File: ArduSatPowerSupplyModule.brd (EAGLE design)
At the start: 95.5 x 90.3 mm, 131 parts, among them IC10 ATMEGA32U4-QFN, IC11 MAX4372F, IC18 TMP102, IC19 TMP102, IC3 MAX17043G+U, IC7 MAX4372F, J1 POWER_JACKPTH, Q1 RJU003N03 N-MOSFET, Q2 MOSFET-PCHANNELSMT2, Q3 BSS138 N-MOSFET, Q4 BSS138 N-MOSFET, Q43 RJU003N03 N-MOSFET, Q44 RJU003N03 N-MOSFET, Q45 RJU003N03 N-MOSFET, Q46 RJU003N03 N-MOSFET, Q5 RJU003N03 N-MOSFET, SW1 SWITCH-DPDT2, SW2 RESET

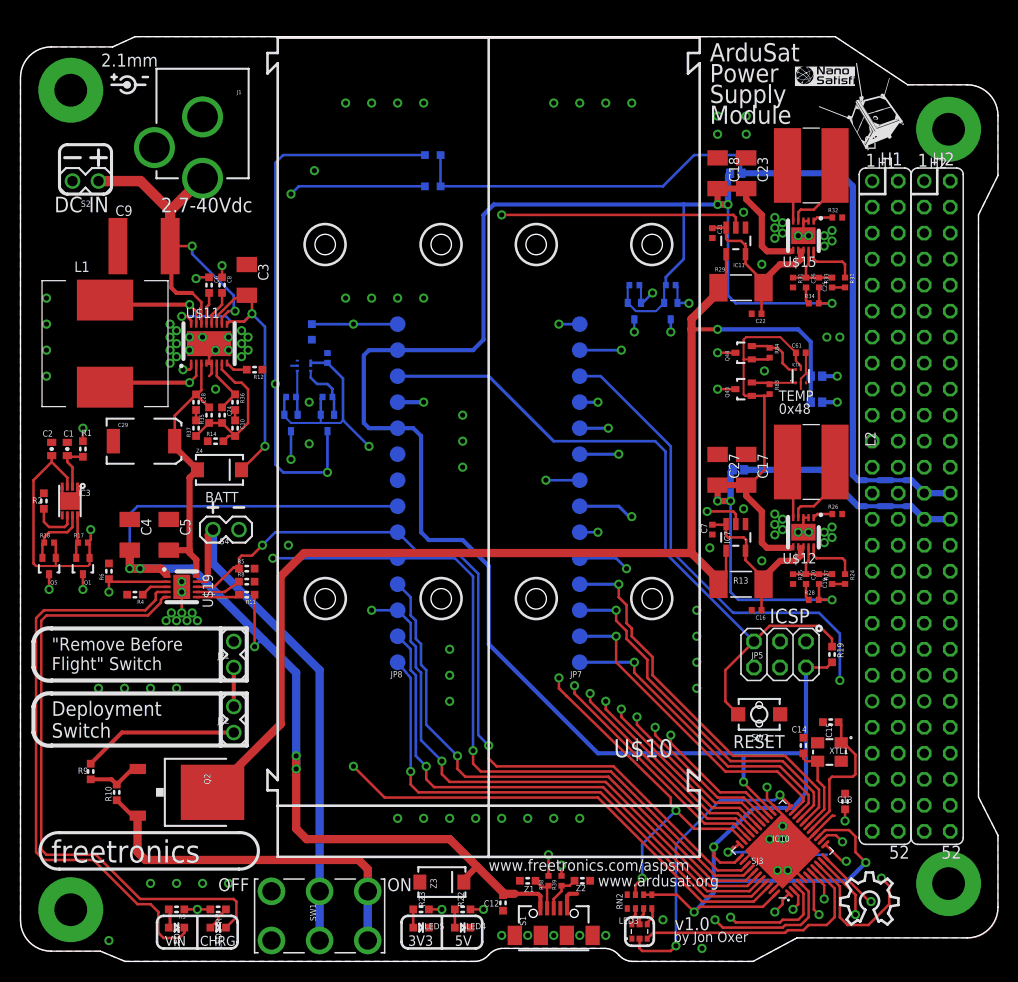
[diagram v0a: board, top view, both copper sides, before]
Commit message: Totally restructured project: single 18650 cell; 0402 parts; shield footprint; dual MCUs in Eleven architecture
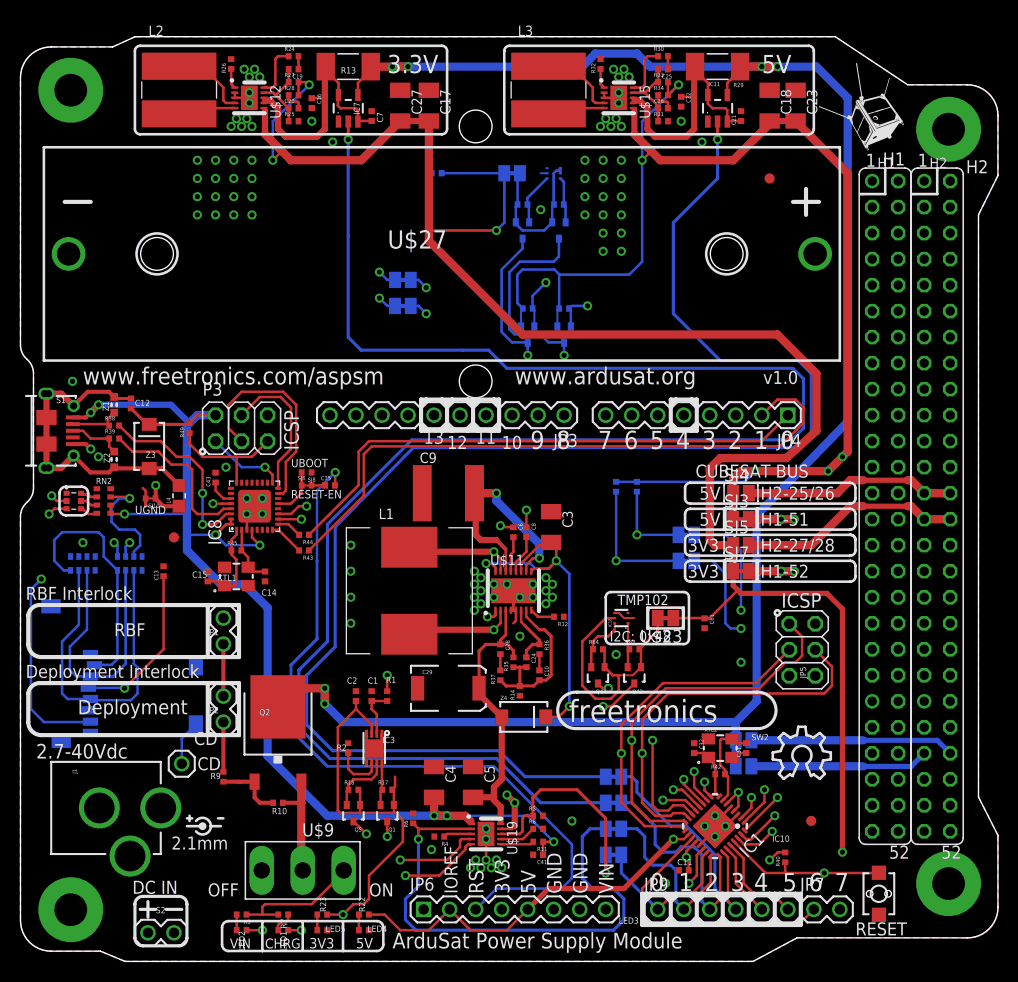
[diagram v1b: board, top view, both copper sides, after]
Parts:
- removed IC10: ATMEGA32U4-QFN, freetronics-jon:QFN-44N
- removed JP8: M14SURFACE, freetronics-jon:1X14SURFACE
- removed R15, R16: 4K7 0603, freetronics-master-v1.1:0603
- removed S4: (no value), freetronics-master-v1:1X02
- removed SW1: SWITCH-DPDT2, freetronics-jon:MS22BNG03
- added C31, C32: 22pF 0603, freetronics-jon:0402C
- added C35: 100nF 0402, freetronics-jon:0402C
- added C41: 100nF 0603, freetronics-jon:0402C
- added C43: 1uF 0603, freetronics-jon:0402C
- added CD: M01PTH, freetronics-2:1X01
- added IC1: AVR-MEGA8-MI, freetronics-jon:MLF32
- added IC8: ATMEGA16U2-MU, freetronics-jon:ATMEL_QFN32
- added JP3: M100.1, freetronics-marc:1X10
- added JP4, JP6: (no value), freetronics-marc:1X08
- added JP9: (no value), freetronics-marc:1X06
- added L4: 0805 INDUCTOR, freetronics-master-v1:0805-LARGE
- added P3: ICSP:USB, pinhead:2X03
- added P4: microSD, freetronics-master-v1:MICRO-SD-SOCKET-PP
- added R40, R49: 10K 0402, freetronics-jon:0402
- added R41: 4K7 0402, freetronics-jon:0402
- added R42, R45: 1M 0402, freetronics-jon:0402
- added R43, R44: 1K 0402, freetronics-jon:0402
- added RN6: 1K, freetronics-master-v1:CAY16
- added RN8: 2K2, freetronics-master-v1:CAY16
- added SJ10: USB_I, freetronics-jon:SJC
- added SJ11: UGND, freetronics-jon:0402SJC
- added SJ6: RESET-EN, freetronics-jon:0402SJC
- added SJ7: 3V3_EN, freetronics-jon:SJC
- added SJ8: UBOOT, freetronics-jon:0402SJO
- added SJ9: DC_I, freetronics-jon:SJC
- added U$14, U$20, U$21, U$23, U$24, U$25, U$26, U$3: SJCN, freetronics-jon:SJC
- added U$27: CELLHOLDER-PCB, freetronics-jon:BH-18650-PC
- added U$28, U$29: FIDUCIAL1X2.5, freetronics-original:FIDUCIAL-1X2.5
- added U$9: SWITCH-SPDT, freetronics-jon:SS-12F100
- added XTL2: 16MHz, freetronics-jon:CRYSTAL-SMD-3X2
- C1, C2: device SparkFun:0402-CAP -> freetronics-jon:0402C
- C10: value 3300pF 0603 -> 3300pF 0402; device freetronics-master-v1.1:0603 -> freetronics-jon:0402C
- C11, C6, C8: value 100nF 0603 -> 100nF 0402; device freetronics-master-v1.1:0603 -> freetronics-jon:0402C
- C12: device freetronics-master-v1.1:0603 -> freetronics-jon:0402C
- C13: value 1uF 0603 -> 100nF 0402; device freetronics-master-v1.1:0603 -> freetronics-jon:0402C
- C14, C15: value 15pF 0603 -> 15pF 0402; device freetronics-master-v1.1:0603 -> freetronics-jon:0402C
- C24: value 27pF 0603 -> 27pF 0402; device freetronics-master-v1.1:0603 -> freetronics-jon:0402C
- C28: value 82pF 0603 -> 82pF 0402; device freetronics-master-v1.1:0603 -> freetronics-jon:0402C
- JP5: value ICSP -> ICSP:MAIN
- JP7: value M14SURFACE -> (none); device freetronics-jon:1X14SURFACE -> freetronics-marc:1X02
- LED1: value RED 0603 -> RED 0402; device freetronics-master-v1:LED-0603 -> freetronics-jon:LED-0402
- LED2: value BLUE 0603 -> BLUE 0402; device freetronics-master-v1:LED-0603 -> freetronics-jon:LED-0402
- LED4, LED5: device freetronics-master-v1:LED-0603 -> freetronics-jon:LED-0402
- Q3, Q4: value BSS138 N-MOSFET -> RJU003N03 N-MOSFET
- R1, R10, R11, R2, R22, R23, R3, R4, R5, R6, R7, R8, R9: device freetronics-master-v1.1:0603 -> freetronics-jon:0402
- R12: value 121K 1% 0603 -> 121K 1% 0402; device freetronics-master-v1.1:0603 -> freetronics-jon:0402
- R14, R37: value 249K 1% 0603 -> 249K 1% 0402; device freetronics-master-v1.1:0603 -> freetronics-jon:0402
- R19: value 10K 0603 -> 4K7 0402; device freetronics-master-v1.1:0603 -> freetronics-jon:0402
- R20, R21: value 10K 0603 -> 10K 0402
- R35: value 1M 1% 0603 -> 1M 1% 0402; device freetronics-master-v1.1:0603 -> freetronics-jon:0402
- R36: value 93.1K 1% 0603 -> 93.1K 1% 0402; device freetronics-master-v1.1:0603 -> freetronics-jon:0402
- S1: value USBSF-MICROB -> USB-6PSMT; device freetronics-jon:USB-MICROB -> freetronics-jon:USB-MICROB-MB05PMXX
- SJ1, SJ2, SJ4, SJ5: device freetronics-master-v1:SJ-TINY -> freetronics-master-v1.1:SJ
- SJ3: value HWB -> 5V_EN; device freetronics-master-v1:SJ-TINY -> freetronics-jon:SJC
- U$10: value CELLHOLDER2 -> FIDUCIAL1X2.5; device freetronics-jon:18650X2 -> freetronics-original:FIDUCIAL-1X2.5
- moved J1 77.3 mm to (0.00, 15.0), turned to 270 degrees
- moved R24 74.2 mm to (26.7, 88.4), turned to 0 degrees
- moved S2 74.1 mm to (15.0, 2.79), turned to 180 degrees
- moved R26 73.7 mm to (20.6, 87.6), turned to 90 degrees
- moved C19 72.4 mm to (26.7, 87.1), turned to 180 degrees
- moved L2 71.6 mm to (15.5, 85.1), turned to 0 degrees
- moved R28 70.8 mm to (26.7, 84.6)
- moved R27 70.6 mm to (26.7, 85.9), turned to 0 degrees
- moved C13 70.2 mm to (14.0, 38.1), turned to 90 degrees
- moved S1 69.9 mm to (2.54, 51.8), turned to 270 degrees
- moved LED3 69.4 mm to (5.21, 45.0), turned to 0 degrees
- moved U$12 68.7 mm to (22.4, 84.3), turned to 270 degrees
- moved C20 68.0 mm to (26.7, 83.3), turned to 0 degrees
- moved R25 66.2 mm to (26.7, 82.0), turned to 0 degrees
- moved C16 65.9 mm to (28.4, 83.8), turned to 270 degrees
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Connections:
- removed net 3V3: C13.2, IC10.6
- removed net A4: IC10.40, JP8.2
- removed net A5: IC10.41, JP8.1
- removed net D10_A11: IC10.30, JP7.11
- removed net D11: IC10.12, JP7.12
- removed net D12: IC10.26, JP7.13
- removed net D13: IC10.32, JP7.14, RN2.3
- removed net D4_A6: IC10.25, JP7.5
- removed net D6_A8: IC10.27, JP7.7
- removed net D7_AIN0: IC10.1, JP7.8
- removed net D8_A9: IC10.28, JP7.9
- removed net D9_A10: IC10.29, JP7.10
- removed net H1L51: H1.51
- removed net H1R52: H1.52
- removed net MISO: IC10.11, JP5.1
- removed net MOSI: IC10.10, JP5.4
- removed net RXLED_SS: IC10.8, LED3.3
- removed net SCK: IC10.9, JP5.3
- removed net TX_LED: IC10.22, LED3.2
- new net +3V3_AS: H1.52, SJ7.2
- new net +5V_AS: H1.51, SJ3.2
- new net A4_SDA: IC1.27, JP3.9, JP9.5, U$26.1
- new net A5_SCL: IC1.28, JP3.10, JP9.6, U$25.1
- new net A6: IC1.19, JP7.1
- new net A7: IC1.22, JP7.2
- new net D10: IC1.14, JP3.3
- new net D11_MOSI: IC1.15, JP3.4, JP5.4, RN6.6
- new net D12_MISO: IC1.16, JP3.5, JP5.1, P4.7
- new net D13_SCK: IC1.17, JP3.6, JP5.3, RN2.3, RN6.7
- new net D4: IC1.2, JP4.5, RN6.5
- new net D6: IC1.10, JP4.7
- new net D7: IC1.11, JP4.8
- new net D8: IC1.12, JP3.1
- new net D9: IC1.13, JP3.2
- new net DC_I: R5.1, SJ9.1, U$19.8
- new net DTR: IC8.13, SJ6.1, SJ8.2
- new net MISO2: IC8.17, P3.1
- new net MOSI2: IC8.16, P3.4
- new net N$13: P4.2, RN6.4, RN8.8
- new net N$24: C32.2, IC1.8, R42.1, XTL2.1
- new net N$34: C43.1, IC8.27
- new net N$38: C12.2, L4.2, S1.FIX1, S1.FIX2, S1.PIN1, S1.PIN2, S1.TAB1, S1.TAB2, Z1.1, Z2.1, Z3.A
- new net N$46: P4.3, RN6.3, RN8.6
- new net N$48: P4.5, RN6.2, RN8.7
- new net N$50: CD.1, P4.CD1
- new net N$51: IC7.2, U$14.1
- new net N$52: C14.2, IC8.2, R45.2, XTL1.3
- new net N$53: IC18.5, Q43.1, Q44.1, R83.2, R84.2, U$23.2
- new net N$54: IC19.4, IC19.5, Q45.1, Q46.1, R85.2, R86.2, U$24.2
- new net N$55: Q3.2, R20.1, U$25.2
- new net N$56: IC8.28, L4.1, S1.GND, SJ11.1
- new net N$57: Q4.2, R21.1, U$26.2
- new net N$60: C35.1, SJ6.2
- new net NC: JP6.1
- new net RESET2: IC8.24, P3.5, R49.1
- new net RXLED: IC8.10, LED3.3
- new net SCK2: IC8.15, P3.3
- new net SYS_SCL: H1.43, U$21.2
- new net SYS_SDA: H1.41, U$20.2
- new net TXLED: IC8.11, LED3.2
- new net USBRXD: IC8.9, R44.2
- new net USBTXD: IC8.8, R43.2
- new net USB_I: R6.1, SJ10.1, U$19.2
- net +5V_SYS: no longer R15.2, R16.2
- net 3.3V: now also C13.1, JP6.4, P4.4, SJ7.1, U$23.1, U$24.1; no longer IC18.5, IC19.4, IC19.5, JP8.11, Q43.1, Q44.1, Q45.1, Q46.1, R83.2, R84.2, R85.2, R86.2
- net 5V: now also IC1.18, IC1.4, IC1.6, JP6.2, JP6.5, R19.2, R40.2, R41.2, SJ3.1; no longer IC10.14, IC10.24, IC10.34, IC10.44, JP8.10, JP8.13, R19.1, RN2.1, RN2.2
- net A0: now also IC1.23, JP9.1, SJ9.2; no longer IC10.36, JP8.6, R5.1, U$19.8
- net A1: now also IC1.24, JP9.2, SJ10.2; no longer IC10.37, JP8.5, R6.1, U$19.2
- net A2: now also IC1.25, JP9.3, U$14.2; no longer IC10.38, IC11.2, JP8.4
- net A3: now also IC1.26, JP9.4, U$3.2; no longer IC10.39, IC7.2, JP8.3
- net AREF: now also IC1.20, JP3.8; no longer IC10.42, JP8.14
- net BAT: now also U$27.+, U$9.1; no longer S4.1, SW1.2, SW1.5
- net D0_RX: now also IC1.30, JP4.1, R44.1; no longer IC10.20, JP7.1
- net D1_TX: now also IC1.31, JP4.2, R43.1; no longer IC10.21, JP7.2
- net D2_SDA: now also IC1.32, JP4.3; no longer IC10.19, JP7.3, Q4.2, R21.1
- net D3_SCL: now also IC1.1, JP4.4; no longer IC10.18, JP7.4, Q3.2, R20.1
- net D5: now also IC1.9, JP4.6; no longer IC10.31, JP7.6
- net GND: now also C13.2, C31.1, C32.1, C41.2, C43.2, IC1.21, IC1.3, IC1.5, IC1.TGND, IC8.3, IC8.EXP, JP3.7, JP6.6, JP6.7, P3.6, P4.6, P4.CD2, P4.GND1, P4.GND2, RN8.1, RN8.2, RN8.3, SJ11.2, SJ8.1, U$27.-, XTL2.2, XTL2.4; no longer C12.2, C13.1, IC10.15, IC10.23, IC10.35, IC10.43, IC10.5, IC10.TGND, JP8.8, JP8.9, S1.FIX1, S1.FIX2, S1.GND, S1.TAB1, S1.TAB2, S4.2, SJ3.2, Z1.1, Z2.1, Z3.A
- net N$10: now also C31.2, IC1.7, R42.2, XTL2.3; no longer IC10.33, SJ3.1
- net N$11: now also IC11.2, U$3.1; no longer C14.2, IC10.17, XTL1.3
- net N$12: now also IC8.1, R45.1; no longer IC10.16
- net N$5: now also U$9.2; no longer SW1.3, SW1.4
- net PVIN: now also JP6.8
- net RD+: now also IC8.29; no longer IC10.4
- net RD-: now also IC8.30; no longer IC10.3
- net RESET: now also C35.2, IC1.29, JP6.3, R40.1; no longer IC10.13, JP8.12, R19.2
- net SCL: now also R41.1, U$21.1; no longer H1.43, R16.1
- net SDA: now also R19.1, U$20.1; no longer H1.41, R15.1
- net USBVCC: now also C41.1, IC8.31, IC8.32, IC8.4, P3.2, R49.2, RN2.1, RN2.2; no longer IC10.2, IC10.7, JP8.7
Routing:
- net N$51: track 0.00 -> 176.4 mm, vias 0 -> 1
- net D12_MISO: track 0.00 -> 158.2 mm, vias 0 -> 2
- net D13_SCK: track 0.00 -> 139.7 mm, vias 0 -> 2
- net N$11: track 9.31 -> 144.3 mm, vias 0 -> 1
- net D11_MOSI: track 0.00 -> 130.0 mm, vias 0 -> 2
- net A5_SCL: track 0.00 -> 128.8 mm, vias 0 -> 1
- net D4: track 0.00 -> 119.5 mm, vias 0 -> 2
- net A4_SDA: track 0.00 -> 115.5 mm, vias 0 -> 1
- net A2: track 132.9 -> 22.8 mm, vias 2 -> 0
- net 3.3V: track 252.4 -> 351.2 mm, vias 7 -> 6
- net SDA: track 185.4 -> 101.9 mm, vias 5 -> 4
- net PVIN: track 47.9 -> 127.9 mm
- net D1_TX: track 31.7 -> 110.7 mm
- net A1: track 97.1 -> 18.6 mm, vias 3 -> 0
- net D0_RX: track 30.8 -> 105.4 mm
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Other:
- outline, holes or cut-outs redrawn
- board text added: "0"
- board text added: "10"
- board text added: "11"
- board text added: "12"
- board text added: "13"
- board text added: "3"
- board text added: "3.3V"
- board text added: "3V3 mA"
- board text added: "4"
- board text added: "5"
- board text added: "5V mA"
- board text added: "6"
- board text added: "7"
- board text added: "8"
- board text added: "9"
- board text added: "A0-3 ISOLATION"
- board text added: "A4/5 ISOLATION"
- board text added: "ArduSat Power Supply Module"
- board text added: "CD"
- board text added: "CUBESAT I2C"
- board text added: "Copyright 2013 Freetronics www.freetronics.com/aspsm"
- board text added: "DC mA"
- board text added: "Deployment"
- board text added: "Deployment Interlock"
- board text added: "H1-41"
- board text added: "H1-43"
- board text added: "H1-51"
- board text added: "H1-52"
- board text added: "H2-25/26"
- board text added: "H2-27/28"
- board text added: "I2C PULLUPS"
- board text added: "I2C: 0x48"
- board text added: "I2C: 0x49"
- board text added: "IOREF"
- board text added: "RBF"
- board text added: "RBF Interlock"
- board text added: "RESET-EN"
- board text added: "RST"
- board text added: "SD CARD D4: nCS D11: MOSI D12: MISO D13: SCK"
- board text added: "SKU: ASPSM"
- board text added: "TMP102"
- board text added: "UBOOT"
- board text added: "UGND"
- board text added: "USB mA"
- board text added: "by Jonathan Oxer"
- board text removed: ""Remove Before Flight" Switch"
- board text removed: "0x48"
- board text removed: "0x49"
- board text removed: "3V3-mA"
- board text removed: "4K7"
- board text removed: "5V-mA"
- board text removed: "AREF"
- board text removed: "ArduSat"
- board text removed: "BATT"
- board text removed: "Copyright 2013 Freetronics Pty Ltd www.freetronics.com/aspsm SKU: ASPSM"
- board text removed: "D0"
- board text removed: "D1"
- board text removed: "D10"
- board text removed: "D11"
- board text removed: "D12"
- board text removed: "D13"
- board text removed: "D2"
- board text removed: "D3"
- board text removed: "D4"
- board text removed: "D5"
- board text removed: "D6"
- board text removed: "D7"
- board text removed: "D8"
- board text removed: "D9"
- board text removed: "DC-mA"
- board text removed: "Deployment Switch"
- board text removed: "HWB"
- board text removed: "Module"
- board text removed: "OPTIONAL I2C BUS PULL-UP RESISTORS"
- board text removed: "Power"
- board text removed: "Supply"
- board text removed: "TEMP"
- board text removed: "USB-mA"
- board text removed: "by Jon Oxer"

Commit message: Routing done, clearances, DRC, overlay. Nearly ready for v1.0 release
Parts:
- removed C61, C62: 100nF 0402, freetronics-jon:0402C
- removed IC18, IC19: TMP102, freetronics-jon:SOT563
- removed P3: ICSP:USB, pinhead:2X03
- removed P4: microSD, freetronics-master-v1:MICRO-SD-SOCKET-PP
- removed Q45, Q46: RJU003N03 N-MOSFET, freetronics-jon:SOT32-3
- removed R49, R84, R85, R86: 10K 0402, freetronics-jon:0402
- removed RN8: 2K2, freetronics-master-v1:CAY16
- removed U$11: LTC3115, freetronics-jon:DFN-16
- removed U$15: LTC3536, freetronics-jon:DFN-10
- removed U$23, U$24: SJCN, freetronics-jon:SJC
- removed U$9: SWITCH-SPDT, freetronics-jon:SS-12F100
- added C30: 22pF 0402, freetronics-jon:0402C
- added C36: 100nF 0402, freetronics-jon:0402C
- added IC10: TMP102, freetronics-jon:SOT563
- added IC2: ATMEGA16U2-MU, freetronics-jon:ATMEL_QFN32
- added IC5: MAX17043G+U, SparkFun:TDFN-8
- added IC6: MAX4372F, freetronics-jon:SOT23-5
- added JP10, JP11: (no value), freetronics-master-v1:1X02
- added Q8, Q9: RJU003N03 N-MOSFET, freetronics-jon:SOT32-3
- added R15: 121K 1% 0402, freetronics-jon:0402
- added R16: 93.1K 1% 0402, freetronics-jon:0402
- added R47, R48: 10K 0402, freetronics-jon:0402
- added RN1: 1K5, resistor-dil:CAY16
- added SJ14, SJ15: SJCN, freetronics-jon:SJC
- added SW1: RESET, freetronics-master-v1:TACTILE_SWITCH_SMD_2PIN_TINY
- C19: value 1nF -> 1nF 0402
- C2: value 10nF -> 10nF 0402
- C21, C33, C7: value 100nF 0603 -> 100nF 0402
- C26: value 100pF -> 100pF 0402
- C31: value 22pF 0603 -> 22pF 0402
- C32: value 22pF 0603 -> 100nF 0402
- IC11: value MAX4372F -> TMP102; device freetronics-jon:SOT23-5 -> freetronics-jon:SOT563
- IC3: value MAX17043G+U -> LTC3115; device SparkFun:TDFN-8 -> freetronics-jon:DFN-16
- IC7: value MAX4372F -> LTC3536; device freetronics-jon:SOT23-5 -> freetronics-jon:DFN-10
- IC8: value ATMEGA16U2-MU -> MAX4372F; device freetronics-jon:ATMEL_QFN32 -> freetronics-jon:SOT23-5
- JP1: value (none) -> ICSP:16U2; device freetronics-master-v1:1X02 -> pinhead:2X03
- JP2: value (none) -> ICSP:328P; device freetronics-master-v1:1X02 -> pinhead:2X03
- JP3: value M100.1 -> (none); device freetronics-marc:1X10 -> freetronics-marc:1X08
- JP4: device freetronics-marc:1X08 -> freetronics-marc:1X06
- JP5: value ICSP:MAIN -> (none); device pinhead:2X03 -> freetronics-marc:1X02
- JP6: value (none) -> M100.1; device freetronics-marc:1X08 -> freetronics-marc:1X10
- JP7: device freetronics-marc:1X02 -> freetronics-marc:1X08
- JP8: value M01PTH -> CD
- JP9: device freetronics-marc:1X06 -> freetronics-master-v1:1X02
- LED4: value BLUE -> BLUE 0402
- LED5: value JADEGREEN -> JADEGREEN 0402
- Q2: value MOSFET-PCHANNELSMT2 -> RJU003N03 N-MOSFET; device freetronics-jon:DPAK -> freetronics-jon:SOT32-3
- Q3: value RJU003N03 N-MOSFET -> MOSFET-PCHANNELSMT2; device freetronics-jon:SOT32-3 -> freetronics-jon:DPAK
- R1: value 1K -> 1M 0402
- R10: value 33K -> 10K 0402
- R11: value 1K -> 2K2 0402
- R12: value 121K 1% 0402 -> 1K 0402
- R13: value 0.1R 2010 -> 4K7 0402; device freetronics-original:R2010 -> freetronics-jon:0402
- R14: value 249K 1% 0402 -> 4K7 0402
- R17: value 10K 0402 -> 1M 1% 0402
- R18: value 10K 0402 -> 249K 1% 0402
- R19: value 4K7 0402 -> 249K 1% 0402
- R2: value 4K7 -> 10K 0402
- R20: value 10K 0402 -> 1K
- R21: value 10K 0402 -> 1.05K 1% 0603
- R22: value 2K2 -> 1.18K 1% 0603
- R23: value 1K -> 1K 1% 0402
- R24: value 49.9K -> 10K 0603
- R25: value 187K -> 2K2 0402
- R26: value 100K -> 1K 0402
- R27: value 845K -> 1K
- R28: value 15K -> 33K
- R29: value 0.1R 2010 -> 1K 0402; device freetronics-original:R2010 -> freetronics-jon:0402
- R3: value 2K2 -> 22R
- R30: value 49.9K -> 4K7 0402
- R31: value 115K -> 10K 0402
- R32: value 100K -> 10K 0402
- R33: value 845K -> 0.1R 2010; device freetronics-jon:0402 -> freetronics-original:R2010
- R34: value 15K -> 100K
- R35: value 1M 1% 0402 -> 49.9K
- R36: value 93.1K 1% 0402 -> 15K 0402
- R37: value 249K 1% 0402 -> 115K 1% 0402
- R38: value 22R -> 845K 1% 0402
- R39: value 22R -> 0.1R 2010; device freetronics-jon:0402 -> freetronics-original:R2010
- R4: value 1K 1% 0603 -> 22R
- R40: value 10K 0402 -> 100K
- R41: value 4K7 0402 -> 49.9K 1% 0402
- R42: value 1M 0402 -> 15K
- R43: value 1K 0402 -> 187K 1% 0402
- R44: value 1K 0402 -> 845K 1% 0402
- R45: value 1M 0402 -> 10K 0402
- R5: value 1.05K 1% 0603 -> 1M 0402
- R6: value 1.18K 1% 0603 -> 10K 0402
- R7: value 1K -> 1K 0402
- R8: value 10K 0603 -> 1K 0402
- R9: value 1K -> 10K 0402
- RN2: value 1K5 -> 2K2; device resistor-dil:CAY16 -> freetronics-master-v1:CAY16
- S2: value (none) -> microSD; device freetronics-master-v1:1X02 -> freetronics-master-v1:MICRO-SD-SOCKET-PP
- SW2: value RESET -> SWITCH-SPDT; device freetronics-master-v1:TACTILE_SWITCH_SMD_2PIN_TINY -> freetronics-jon:SS-12F100
- moved R40 94.5 mm to (20.6, 87.6)
- moved R26 83.2 mm to (25.7, 4.57), turned to 0 degrees
- moved R24 79.1 mm to (50.5, 13.0)
- moved R42 78.3 mm to (26.7, 84.6)
- moved R25 77.6 mm to (21.6, 4.57), turned to 180 degrees
- moved R30 74.2 mm to (32.0, 20.8), turned to 270 degrees
- moved R32 73.9 mm to (35.8, 16.8), turned to 0 degrees
- moved R31 71.9 mm to (32.5, 16.8)
- moved R29 69.4 mm to (35.8, 25.9), turned to 90 degrees
- moved R28 69.1 mm to (25.1, 15.5), turned to 180 degrees
- moved R27 68.2 mm to (19.8, 18.0), turned to 270 degrees
- moved R38 63.2 mm to (62.7, 85.9)
- moved R35 61.0 mm to (62.7, 88.4), turned to 0 degrees
- moved JP2 56.7 mm to (76.3, 30.4)
- moved SW2 56.3 mm to (27.6, 8.89), turned to 180 degrees
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- renumbered C41 to C33, C43 to C34, CD to JP8, J1 to S3, Q43 to Q6, Q44 to Q7, R83 to R46, RN6 to RN3, U$12 to IC9, U$14 to SJ19, U$19 to IC4, U$20 to SJ12, U$21 to SJ13, U$25 to SJ16, U$26 to SJ17, U$27 to BAT1, U$3 to SJ18
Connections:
- net 3.3V: now also C35.1, C36.1, IC5.3, JP3.4, Q4.1, R12.1, R31.2, R32.2, R42.2, R44.2, S2.4, SJ14.1, SJ15.1; no longer C61.1, C62.1, IC3.3, JP6.4, P4.4, Q1.1, R17.2, R18.2, R23.1, R27.2, R28.2, U$23.1, U$24.1
- net 3V3SENSED: now also IC8.3, IC8.5, R39.2; no longer IC7.3, IC7.5, R13.2
- net 5V: now also IC7.6, JP2.2, JP3.2, JP3.5, Q1.1, Q2.1, R10.2, R11.1, R13.2, R14.2, R36.2, R38.2, R6.2, R9.2; no longer JP5.2, JP6.2, JP6.5, Q3.1, Q4.1, R19.2, R20.2, R21.2, R22.1, R33.2, R34.2, R40.2, R41.2, U$15.6
- net 5VSENSED: now also IC6.3, IC6.5, IC7.7, IC7.8, R33.2; no longer IC11.3, IC11.5, R29.2, U$15.7, U$15.8
- net A0: now also JP4.1; no longer JP9.1
- net A1: now also JP4.2; no longer JP9.2
- net A2: now also JP4.3; no longer JP9.3
- net A3: now also JP4.4; no longer JP9.4
- net A4_SDA: now also JP4.5, JP6.9; no longer JP3.9, JP9.5
- net A5_SCL: now also JP4.6, JP6.10; no longer JP3.10, JP9.6
- net A6: now also JP5.1; no longer JP7.1
- net A7: now also JP5.2; no longer JP7.2
- net AREF: now also JP6.8; no longer JP3.8
- net BAT: now also R25.1, R26.1, R29.2, SW2.1; no longer R1.2, R3.1, R7.1, U$9.1
- net CELL: now also IC5.2, R29.1; no longer IC3.2, R1.1
- net D+: now also R4.1; no longer R39.1
- net D-: now also R3.1; no longer R38.1
- net D0_RX: now also JP7.1, R8.1; no longer JP4.1, R44.1
- net D10: now also JP6.3; no longer JP3.3
- net D11_MOSI: now also JP2.4, JP6.4; no longer JP3.4, JP5.4
- net D12_MISO: now also JP2.1, JP6.5, S2.7; no longer JP3.5, JP5.1, P4.7
- net D13_SCK: now also JP2.3, JP6.6, RN1.3; no longer JP3.6, JP5.3, RN2.3
- net D1_TX: now also JP7.2, R7.1; no longer JP4.2, R43.1
- net D2_SDA: now also JP7.3; no longer JP4.3
- net D3_SCL: now also JP7.4; no longer JP4.4
- net D4: now also JP7.5; no longer JP4.5
- net D5: now also JP7.6; no longer JP4.6
- net D6: now also JP7.7; no longer JP4.7
- net D7: now also JP7.8; no longer JP4.8
- net D8: now also JP6.1; no longer JP3.1
- net D9: now also JP6.2; no longer JP3.2
- net DC_I: now also R21.1; no longer R5.1
- net DTR: now also IC2.13; no longer IC8.13
- net GND: now also C30.1, C35.2, C36.2, IC10.2, IC10.4, IC11.2, IC2.3, IC2.EXP, IC3.5, IC3.TGND, IC5.1, IC5.4, IC5.EP, IC6.1, IC7.2, IC7.3, IC7.TGND, IC8.1, JP1.6, JP10.1, JP2.6, JP3.6, JP9.1, R15.1, R18.1, R21.2, R22.2, R23.2, R24.2, R30.1, R34.2, R37.2, R40.2, R43.2, RN2.1, RN2.2, RN2.3, S2.6, S2.CD2, S2.GND1, S2.GND2, SW1.1; no longer C32.1, C61.2, C62.2, IC11.1, IC18.2, IC18.4, IC19.2, IC3.1, IC3.EP, IC7.1, IC8.3, IC8.EXP, JP1.1, JP5.6, JP6.6, P3.6, P4.6, P4.CD2, P4.GND1, P4.GND2, R12.1, R14.1, R2.1, R25.2, R26.2, R31.2, R32.2, R4.2, R5.2, R6.2, R8.2, RN8.1, RN8.2, RN8.3, S2.1, SW2.1, U$11.4, U$11.5, U$11.TGND, U$15.2, U$15.3, U$15.TGND
- net MISO2: now also IC2.17, JP1.1; no longer IC8.17, P3.1
- net MOSI2: now also IC2.16, JP1.4; no longer IC8.16, P3.4
- net N$1: now also R12.2; no longer R23.2
- net N$10: now also C30.2, R5.2; no longer C31.2, R42.2
- net N$10001: now also IC10.6, R45.1; no longer IC18.6, R84.1
- net N$10002: now also IC11.6, Q9.2, R47.1; no longer IC19.6, Q46.2, R86.1
- net N$10003: now also IC11.1, Q8.2, R48.1; no longer IC19.1, Q45.2, R85.1
- net N$11: now also IC6.2; no longer IC11.2
- net N$12: now also IC2.1, R1.1; no longer IC8.1, R45.1
- net N$13: now also RN2.8, S2.2; no longer P4.2, RN8.8
- net N$14: now also RN1.6; no longer RN2.6
- net N$15: now also R41.1; no longer R24.1
- net N$16: now also RN1.7; no longer RN2.7
- net N$17: now also RN1.8; no longer RN2.8
- net N$2: now also JP10.2, JP11.1; no longer JP1.2, JP2.1
- net N$20: now also R24.1; no longer R8.1
- net N$21: now also R40.1; no longer R26.1
- net N$22: now also IC7.4; no longer U$15.4
- net N$23: now also R41.2; no longer R24.2
- net N$24: now also C31.2, R5.1; no longer C32.2, R42.1
- net N$248: now also R26.2; no longer R7.2
- net N$25: now also R42.1; no longer R28.1
- net N$26: now also R43.1, R44.1; no longer R25.1, R27.1
- net N$28: now also IC7.5; no longer U$15.5
- net N$29: now also IC7.1, R34.1; no longer R32.1, U$15.1
- net N$3: now also R25.2; no longer R3.2
- net N$30: now also R35.2; no longer R30.2
- net N$31: now also IC7.10, R35.1; no longer R30.1, U$15.10
- net N$32: now also R36.1; no longer R34.1
- net N$33: now also IC7.9, R37.1, R38.1; no longer R31.1, R33.1, U$15.9
- net N$34: now also IC2.27; no longer IC8.27
- net N$35: now also R23.1; no longer R4.1
- net N$36: now also R20.2; no longer R11.2
- net N$37: now also R16.2; no longer R36.2
- net N$39: now also IC3.11, IC3.16, IC3.9; no longer U$11.11, U$11.16, U$11.9
- net N$4: now also JP11.2, R27.1; no longer JP2.2, R9.1
- net N$40: now also IC3.13; no longer U$11.13
- net N$41: now also IC3.12; no longer U$11.12
- net N$42: now also IC3.15; no longer U$11.15
- net N$43: now also IC3.2; no longer U$11.2
- net N$44: now also IC3.6, R16.1; no longer R36.1, U$11.6
- net N$45: now also IC3.7, R17.1, R18.2, R19.1; no longer R14.2, R35.1, R37.1, U$11.7
- net N$46: now also RN2.6, S2.3; no longer P4.3, RN8.6
- net N$47: now also IC3.8, R15.2; no longer R12.2, U$11.8
- net N$48: now also RN2.7, S2.5; no longer P4.5, RN8.7
- net N$49: now also R19.2; no longer R37.2
- net N$5: now also Q3.3, R28.1, SW2.2; no longer Q2.3, R10.1, U$9.2
- net N$50: now also S2.CD1; no longer P4.CD1
- net N$51: now also IC8.2; no longer IC7.2
- net N$52: now also IC2.2, R1.2; no longer IC8.2, R45.2
- net N$53: now also IC10.5, R45.2, SJ14.2; no longer IC18.5, R84.2, U$23.2
- net N$54: now also IC11.4, IC11.5, Q8.1, Q9.1, R47.2, R48.2, SJ15.2; no longer IC19.4, IC19.5, Q45.1, Q46.1, R85.2, R86.2, U$24.2
- net N$55: now also Q1.2, R9.1; no longer Q3.2, R20.1
- net N$56: now also IC2.28; no longer IC8.28
- net N$57: now also Q2.2, R10.1; no longer Q4.2, R21.1
- net N$6: now also R11.2; no longer R22.2
- net N$60: now also C32.1; no longer C35.1
- net N$7: now also Q3.1, R27.2, R28.2; no longer Q2.1, R10.2, R9.2
- net N$8: now also IC5.8, Q4.2, R32.1; no longer IC3.8, Q1.2, R17.1
- net N$9: now also IC5.7, R31.1; no longer IC3.7, R18.1
- net N$9999: now also IC10.1; no longer IC18.1
- net NC: now also JP3.1; no longer JP6.1
- net PVIN: now also IC3.1, IC3.10, IC3.14, JP3.8, JP9.2; no longer JP6.8, S2.2, U$11.1, U$11.10, U$11.14
- net PVOUT: now also IC3.3, R17.2; no longer R35.2, U$11.3
- net QST: now also IC5.6, R30.2; no longer IC3.6, R2.2
- net RD+: now also IC2.29, R4.2; no longer IC8.29, R39.2
- net RD-: now also IC2.30, R3.2; no longer IC8.30, R38.2
- net RESET: now also C32.2, JP2.5, JP3.3, R6.1, SW1.2; no longer C35.2, JP5.5, JP6.3, R40.1, SW2.2
- net RESET2: now also IC2.24, JP1.5, R2.1; no longer IC8.24, P3.5, R49.1
- net RXLED: now also IC2.10; no longer IC8.10
- net SCK2: now also IC2.15, JP1.3; no longer IC8.15, P3.3
- net SCL: now also Q1.3, Q8.3, R13.1; no longer Q3.3, Q45.3, R41.1
- net SDA: now also Q2.3, Q9.3, R14.1; no longer Q1.3, Q46.3, R19.1
- net TXLED: now also IC2.11; no longer IC8.11
- net USBRXD: now also IC2.9, R8.2; no longer IC8.9, R44.2
- net USBTXD: now also IC2.8, R7.2; no longer IC8.8, R43.2
- net USBVCC: now also IC2.31, IC2.32, IC2.4, JP1.2, R2.2, R20.1, RN1.1, RN1.2; no longer IC8.31, IC8.32, IC8.4, P3.2, R11.1, R49.2, RN2.1, RN2.2
- net USB_I: now also R22.1; no longer R6.1
- net VBATT: now also IC6.4, IC8.4, Q3.2, R33.1, R39.1; no longer IC11.4, IC7.4, Q2.2, R13.1, R29.1
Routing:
- net 3.3V: track 351.2 -> 349.1 mm
- net N$53: track 26.0 -> 27.0 mm
- net N$9999: track 4.44 -> 4.95 mm
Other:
- board text added: "(DC IN)"
- board text added: "ANALOG"
- board text added: "AREF"
- board text added: "CUBESAT BUS H1-41: SDA H1-43: SCL H2-25: 5V H2-26: 5V H2-27: 3V3 H2-28: 3V3 H2-29: GND H2-30: GND H2-32: GND H2-45: VBATT45 H2-46: VBATT46"
- board text added: "DIGITAL"
- board text added: "I2C ADDRESSES 0x36: MAX17043G+U 0x48: TMP102 (TOP) 0x49: TMP102 (BOT)"
- board text added: "SW1"
- board text added: "~"
- board text removed: "H1-41: SDA H1-43: SCL H2-25: 5V H2-26: 5V H2-27: 3V3 H2-28: 3V3 H2-29: GND H2-30: GND H2-32: GND H2-45: VBATT45 H2-46: VBATT46"
- board text removed: "SW2"
- board text removed: "TEMP SENSOR I2C ADDRESSES TOP: 0x48 BOT: 0x49"
